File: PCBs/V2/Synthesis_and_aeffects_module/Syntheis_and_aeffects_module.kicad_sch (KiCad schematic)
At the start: 19 parts, among them J1 AudioJack3_SwitchTR, U1 STM32H750VBTx

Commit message: pcb progress
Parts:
- added C(c)output1, C(c)output2: 220uf, symbol Device:C
- added C6(decoupleamp)1: 0.1uf, Capacitor_SMD:C_0603_1608Metric_Pad1.08x0.95mm_HandSolder, symbol Device:C
- added Cbypass1: 0.1uf(LOW ESR - or 0.47uf), symbol Device:C
- added Cinput1, Cinput2: 0.47uf, symbol Device:C
- added Debug1, Debug2, Debug3, Debug4: Conn_01x01, TestPoint:TestPoint_Pad_1.5x1.5mm, symbol Connector_Generic:Conn_01x01
- added J2: IN, Connector_PinHeader_2.54mm:PinHeader_1x05_P2.54mm_Vertical, symbol Connector_Generic:Conn_01x05
- added J3: OUT, Connector_PinHeader_2.54mm:PinHeader_1x05_P2.54mm_Vertical, symbol Connector_Generic:Conn_01x05
- added Rf(40k)1, Rf(40k)2: 40k, symbol Device:R
- added Ri(20k)1, Ri(20k)2: 20k, symbol Device:R
- added U2: TPA6110A2DGN, Package_SO:HVSSOP-8-1EP_3x3mm_P0.65mm_EP1.57x1.89mm, symbol Amplifier_Audio:TPA6110A2DGN
- C1, C2, C3, C4, C5, C8, C9: value C -> 0.1uf; footprint Capacitor_THT:CP_Radial_D5.0mm_P2.00mm -> Capacitor_SMD:C_0603_1608Metric_Pad1.08x0.95mm_HandSolder
- C6(VCAP)1: renamed from C6; footprint Capacitor_THT:CP_Radial_D5.0mm_P2.00mm -> Capacitor_SMD:C_0603_1608Metric_Pad1.08x0.95mm_HandSolder
- C7(VCAP)2: renamed from C7; footprint Capacitor_THT:CP_Radial_D5.0mm_P2.00mm -> Capacitor_SMD:C_0603_1608Metric_Pad1.08x0.95mm_HandSolder
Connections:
- net DAC_OUT1: now also Cinput2.1, Debug1.1 (Pin_1); no longer J1.T
- net DAC_OUT2: now also Cinput1.1, Debug2.1 (Pin_1); no longer J1.R
- net GNDPWR: now also Cbypass1.2, J2.1 (Pin_1), J3.1 (Pin_1), U2.2 (GND), U2.3 (SHDN), U2.9 (GND)
- net MISC_3: now also U1.77 (PA15); no longer U1.79 (PC11)
- net VCC: now also J2.2 (Pin_2), J3.2 (Pin_2), U2.6 (VDD)
- net USART1_COMM_INPUT_RX: now reaches U1.46 (PB10)
- net USART1_COMM_INPUT_RX: now also J2.4 (Pin_4)
- net USART1_MIDI_TX: now reaches U1.68 (PA9)
- net USART1_MIDI_TX: now also J3.5 (Pin_5)
- net USART1_MIDI_RX: now reaches U1.69 (PA10)
- net USART1_MIDI_RX: now also J2.5 (Pin_5)
- net USART3_MIDI_TX: now reaches U1.78 (PC10)
- net USART2_COMM_OUTPUT_TX: now reaches U1.86 (PD5)
- net USART2_COMM_OUTPUT_TX: now also J3.4 (Pin_4)
- net USART2_COMM_OUTPUT_RX: now reaches U1.87 (PD6)
- net USART2_COMM_OUTPUT_RX: now also J3.3 (Pin_3)
- net USART1_COMM_INPUT_TX: now reaches U1.96 (PB9)
- net USART1_COMM_INPUT_TX: now also J2.3 (Pin_3)
- net at J1.RN: now also C(c)output2.2
- net UART5_COMM_RX: no longer names the net of U1.51 (PB12)
- net UART5_COMM_TX: no longer names the net of U1.52 (PB13)
- net UART_MIDI_RX: no longer names the net of U1.70 (PA11)
- net UART_MIDI_TX: no longer names the net of U1.71 (PA12)
- new net: Cinput2.2, Rf(40k)1.1, Ri(20k)2.1, U2.8 (IN1-)
- new net: C(c)output1.1, Debug3.1 (Pin_1), Rf(40k)1.2, U2.7 (VO1)
- new net: Cbypass1.1, Ri(20k)1.1, Ri(20k)2.2, U2.1 (BYPASS)
- new net: C(c)output2.1, Debug4.1 (Pin_1), Rf(40k)2.2, U2.5 (VO2)
- new net: Cinput1.2, Rf(40k)2.1, Ri(20k)1.2, U2.4 (IN2-)
- new net: C(c)output1.2, J1.T
- new net USART3_MIDI_RX: U1.79 (PC11)
- no-connect marks 74 -> 70
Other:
- note added: "Switchbox communication IN"
- note removed: "For communication with switch boxes, other modules, etc"
- moved on the sheet: J1, Programmer1

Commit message: schematic progress
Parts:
- 1k3, 1k4: footprint Resistor_THT:R_Axial_DIN0204_L3.6mm_D1.6mm_P7.62mm_Horizontal -> Resistor_SMD:R_0603_1608Metric_Pad0.98x0.95mm_HandSolder
- C(c)output1, C(c)output2: footprint (none) -> Capacitor_THT:CP_Radial_D5.0mm_P2.00mm
- Cbypass1: value 0.1uf(LOW ESR - or 0.47uf) -> 0.47uf(LOW ESR); footprint (none) -> Capacitor_SMD:C_0603_1608Metric_Pad1.08x0.95mm_HandSolder
- Cinput1, Cinput2: footprint (none) -> Capacitor_SMD:C_0603_1608Metric_Pad1.08x0.95mm_HandSolder
- Rf(40k)1, Rf(40k)2: footprint (none) -> Resistor_THT:R_Axial_DIN0207_L6.3mm_D2.5mm_P10.16mm_Horizontal
- Ri(20k)1: renamed from Ri(20k)2; footprint (none) -> Resistor_THT:R_Axial_DIN0207_L6.3mm_D2.5mm_P10.16mm_Horizontal
- Ri(20k)2: renamed from Ri(20k)1; footprint (none) -> Resistor_THT:R_Axial_DIN0207_L6.3mm_D2.5mm_P10.16mm_Horizontal
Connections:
- net GNDPWR: no longer U2.3 (SHDN)
- net VCC: now also C6(decoupleamp)1.1, U2.3 (SHDN); no longer U2.6 (VDD)
- net at Cinput2.2, Rf(40k)1.1, Ri(20k)1.1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: now also Cinput1.2, Rf(40k)2.1, Ri(20k)2.2, U2.4 (IN2-)
- net at C6(decoupleamp)1.2: now also U2.6 (VDD)
- net at C(c)output2.2: now also J1.R; no longer J1.RN
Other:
- note added: "0.1uf also acceptable but will have more pop on start"
- note added: "TODO: Switch to all SMD, some are tht for convinience"
- moved on the sheet: C6(decoupleamp)1, Cinput1, Cinput2, Debug1, Debug2, Rf(40k)1, Rf(40k)2

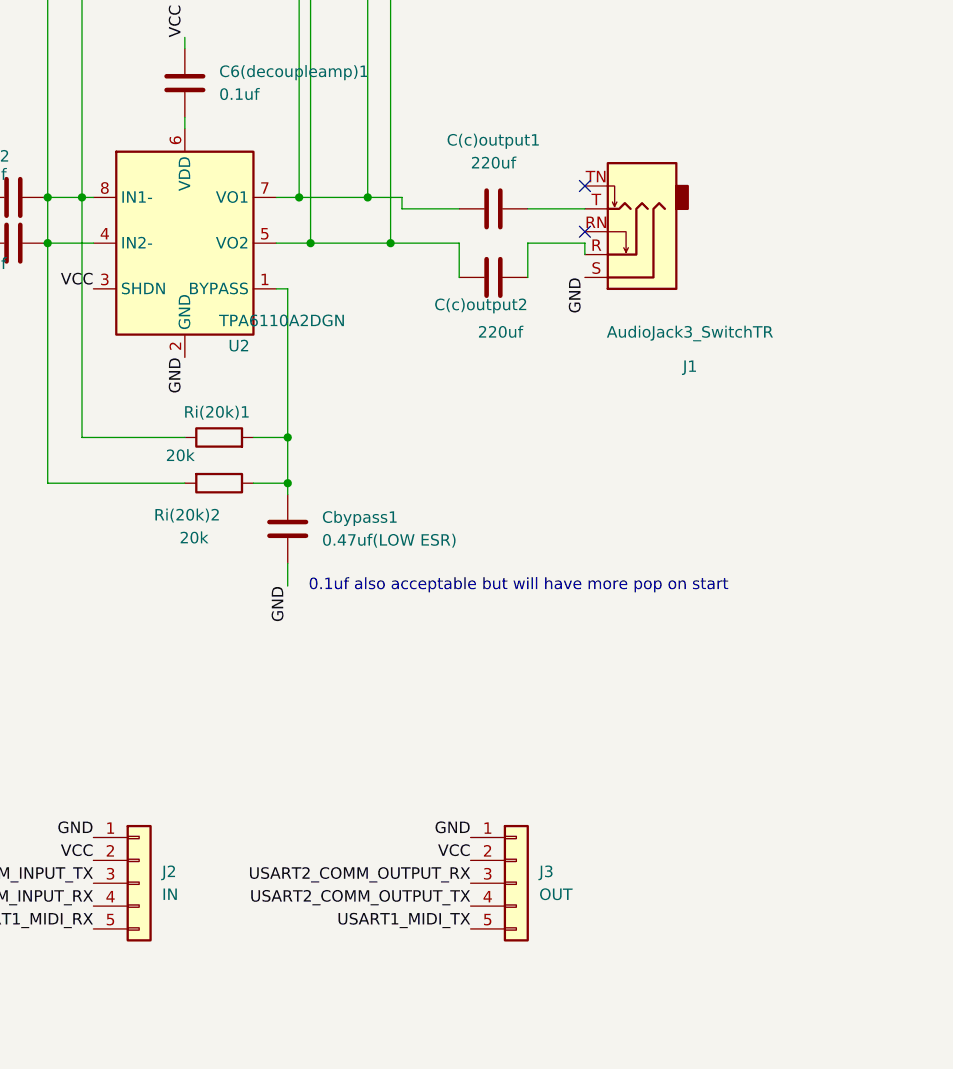
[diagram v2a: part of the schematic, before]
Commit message: remove adiojack from schematic, replace with pin headers
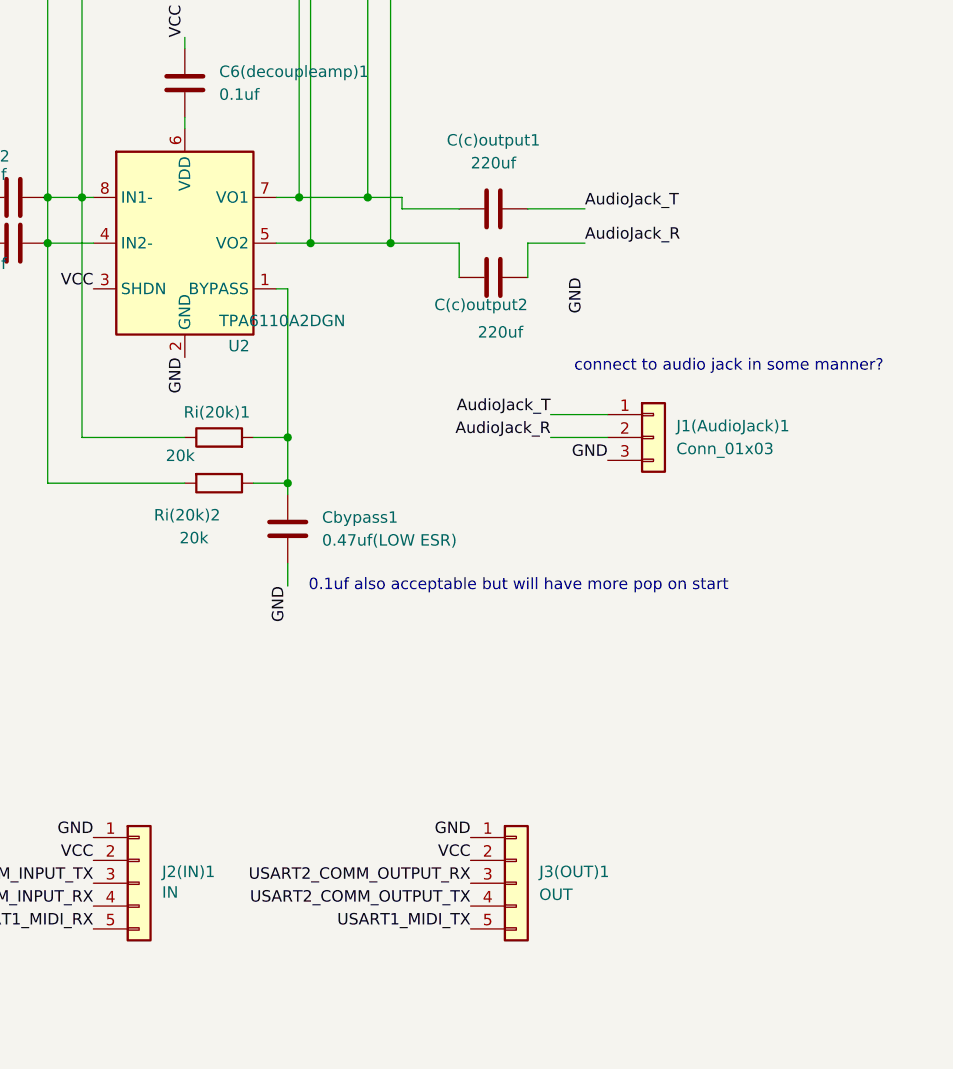
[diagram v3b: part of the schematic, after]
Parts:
- removed J1: AudioJack3_SwitchTR, Connector_Audio:Jack_3.5mm_CUI_SJ1-3525N_Horizontal, symbol Connector_Audio:AudioJack3_SwitchTR
- added J1(AudioJack)1: Conn_01x03, Connector_PinHeader_2.54mm:PinHeader_1x03_P2.54mm_Vertical, symbol Connector_Generic:Conn_01x03
- renumbered J2 to J2(IN)1, J3 to J3(OUT)1
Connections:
- net GNDPWR: now also J1(AudioJack)1.3 (Pin_3)
- net AudioJack_R: now reaches C(c)output2.2
- net AudioJack_R: now also J1(AudioJack)1.2 (Pin_2)
- net AudioJack_T: now reaches C(c)output1.2
- net AudioJack_T: now also J1(AudioJack)1.1 (Pin_1)
- no-connect marks 70 -> 68
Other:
- note added: "connect to audio jack in some manner?"
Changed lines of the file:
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@@
 		)
 	)
+	(text "connect to audio jack in some manner?\n"
+		(exclude_from_sim no)
+		(at 277.622 87.376 0)
+		(effects
+			(font
+				(size 1.27 1.27)
+			)
+		)
+	)
 	(text "TODO: Switch to all SMD, some are tht for convinience\n"
 		(exclude_from_sim no)
@@
 	)
 	(no_connect
-		(at 261.62 72.39)
-	)
-	(no_connect
 		(at 125.73 54.61)
 	)
@@
 	)
 	(no_connect
-		(at 261.62 67.31)
-	)
-	(no_connect
 		(at 80.01 77.47)
 	)
@@
 	(wire
 		(pts
+			(xy 257.81 92.71) (xy 264.16 92.71)
+		)
+		(stroke
+			(width 0)
+			(type default)
+		)
+	)
+	(wire
+		(pts
 			(xy 229.87 35.56) (xy 229.87 68.58)
 		)
@@
 	(wire
 		(pts
-			(xy 261.62 73.66) (xy 261.62 74.93)
-		)
-		(stroke
-			(width 0)
-			(type default)
-		)
-	)
-	(wire
-		(pts
 			(xy 71.12 158.75) (xy 71.12 161.29)
 		)
@@
 	(wire
 		(pts
+			(xy 257.81 95.25) (xy 264.16 95.25)
+		)
+		(stroke
+			(width 0)
+			(type default)
+		)
+	)
+	(wire
+		(pts
 			(xy 224.79 100.33) (xy 228.6 100.33)
 		)
@@
 		)
 	)
+	(label "AudioJack_T"
+		(at 257.81 92.71 180)
+		(effects
+			(font
+				(size 1.27 1.27)
+			)
+			(justify right bottom)
+		)
+	)
 	(label "USART1_MIDI_RX"
 		(at 125.73 72.39 0)
@@
 		)
 	)
+	(label "GND"
+		(at 264.16 97.79 180)
+		(effects
+			(font
+				(size 1.27 1.27)
+			)
+			(justify right bottom)
+		)
+	)
 	(label "USART1_MIDI_TX"
 		(at 125.73 69.85 0)
@@
 		)
 	)
+	(label "AudioJack_R"
+		(at 261.62 73.66 0)
+		(effects
+			(font
+				(size 1.27 1.27)
+			)
+			(justify left bottom)
+		)
+	)
+	(label "AudioJack_R"
+		(at 257.81 95.25 180)
+		(effects
+			(font
+				(size 1.27 1.27)
+			)
+			(justify right bottom)
+		)
+	)
 	(label "GND"
 		(at 228.6 111.76 270)
@@
 		)
 	)
+	(label "AudioJack_T"
+		(at 261.62 69.85 0)
+		(effects
+			(font
+				(size 1.27 1.27)
+			)
+			(justify left bottom)
+		)
+	)
 	(label "GND"
 		(at 100.33 24.13 90)
@@
 		(on_board yes)
 		(dnp no)
-		(fields_autoplaced yes)
-		(property "Reference" "J2"
+		(property "Reference" "J2(IN)1"
 			(at 214.63 143.5099 0)
 			(effects
@@
 		)
 		(property "Value" "IN"
-			(at 214.63 146.0499 0)
+			(at 214.63 145.796 0)
 			(effects
 				(font
@@
 			(project ""
 				(path "/edf9ac54-8c23-46ef-867e-bfab8959c07a"
-					(reference "J2")
+					(reference "J2(IN)1")
 					(unit 1)
 				)
@@
 	)
 	(symbol
-		(lib_id "Connector_Audio:AudioJack3_SwitchTR")
-		(at 266.7 74.93 180)
-		(unit 1)
-		(exclude_from_sim no)
-		(in_bom yes)
-		(on_board yes)
-		(dnp no)
-		(property "Reference" "J1"
-			(at 273.304 87.376 0)
-			(effects
-				(font
-					(size 1.27 1.27)
-				)
-			)
-		)
-		(property "Value" "AudioJack3_SwitchTR"
-			(at 273.304 83.566 0)
-			(effects
-				(font
-					(size 1.27 1.27)
-				)
-			)
-		)
-		(property "Footprint" "Connector_Audio:Jack_3.5mm_CUI_SJ1-3525N_Horizontal"
-			(at 266.7 74.93 0)
-			(effects
-				(font
-					(size 1.27 1.27)
-				)
-				(hide yes)
-			)
-		)
-		(property "Datasheet" "~"
-			(at 266.7 74.93 0)
-			(effects
-				(font
-					(size 1.27 1.27)
-				)
-				(hide yes)
-			)
-		)
-		(property "Description" "Audio Jack, 3 Poles (Stereo / TRS), Switched TR Poles (Normalling)"
-			(at 266.7 74.93 0)
-			(effects
-				(font
-					(size 1.27 1.27)
-				)
-				(hide yes)
-			)
-		)
-		(pin "R"
-		)
-		(pin "RN"
-		)
-		(pin "TN"
-		)
-		(pin "T"
-		)
-		(pin "S"
-		)
-		(instances
-			(project ""
-				(path "/edf9ac54-8c23-46ef-867e-bfab8959c07a"
-					(reference "J1")
-					(unit 1)
-				)
-			)
-		)
-	)
-	(symbol
 		(lib_id "Device:C")
 		(at 102.87 27.94 0)
@@
 	)
 	(symbol
+		(lib_id "Connector_Generic:Conn_01x03")
+		(at 269.24 95.25 0)
+		(unit 1)
+		(exclude_from_sim no)
+		(in_bom yes)
+		(on_board yes)
+		(dnp no)
+		(fields_autoplaced yes)
+		(property "Reference" "J1(AudioJack)1"
+			(at 271.78 93.9799 0)
+			(effects
+				(font
+					(size 1.27 1.27)
+				)
+				(justify left)
+			)
+		)
+		(property "Value" "Conn_01x03"
+			(at 271.78 96.5199 0)
+			(effects
+				(font
+					(size 1.27 1.27)
+				)
+				(justify left)
+			)
+		)
+		(property "Footprint" "Connector_PinHeader_2.54mm:PinHeader_1x03_P2.54mm_Vertical"
+			(at 269.24 95.25 0)
+			(effects
+				(font
+					(size 1.27 1.27)
+				)
+				(hide yes)
+			)
+		)
+		(property "Datasheet" "~"
+			(at 269.24 95.25 0)
+			(effects
+				(font
+					(size 1.27 1.27)
+				)
+				(hide yes)
+			)
+		)
+		(property "Description" "Generic connector, single row, 01x03, script generated (kicad-library-utils/schlib/autogen/connector/)"
+			(at 269.24 95.25 0)
+			(effects
+				(font
+					(size 1.27 1.27)
+				)
+				(hide yes)
+			)
+		)
+		(pin "1"
+		)
+		(pin "2"
+		)
+		(pin "3"
+		)
+		(instances
+			(project ""
+				(path "/edf9ac54-8c23-46ef-867e-bfab8959c07a"
+					(reference "J1(AudioJack)1")
+					(unit 1)
+				)
+			)
+		)
+	)
+	(symbol
 		(lib_id "power:PWR_FLAG")
 		(at 140.97 48.26 270)
@@
 		(dnp no)
 		(fields_autoplaced yes)
-		(property "Reference" "J3"
+		(property "Reference" "J3(OUT)1"
 			(at 256.54 143.5099 0)
 			(effects
@@
 			(project "Syntheis_and_aeffects_module"
 				(path "/edf9ac54-8c23-46ef-867e-bfab8959c07a"
-					(reference "J3")
+					(reference "J3(OUT)1")
 					(unit 1)
 				)
